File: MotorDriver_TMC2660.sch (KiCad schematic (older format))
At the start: 16 parts, among them U4 TMC2660

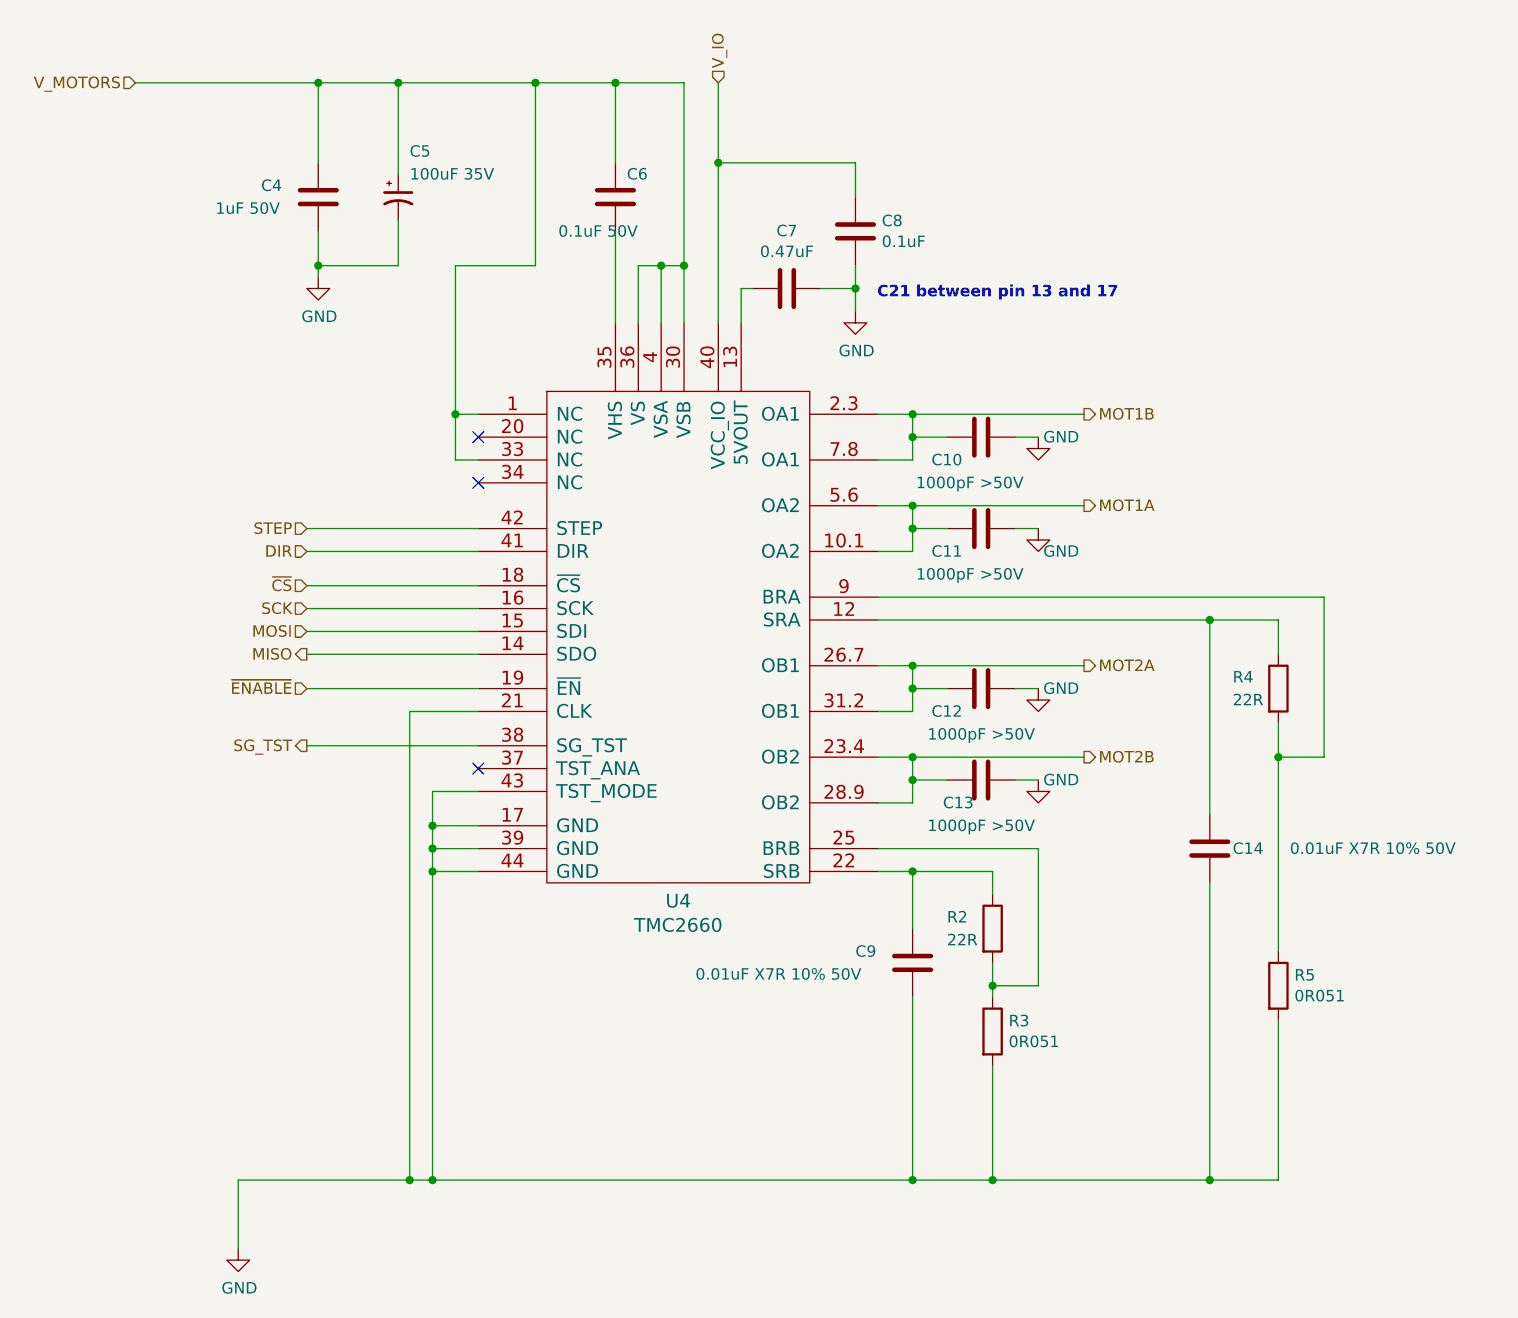
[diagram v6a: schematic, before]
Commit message: Routed most of the power traces.
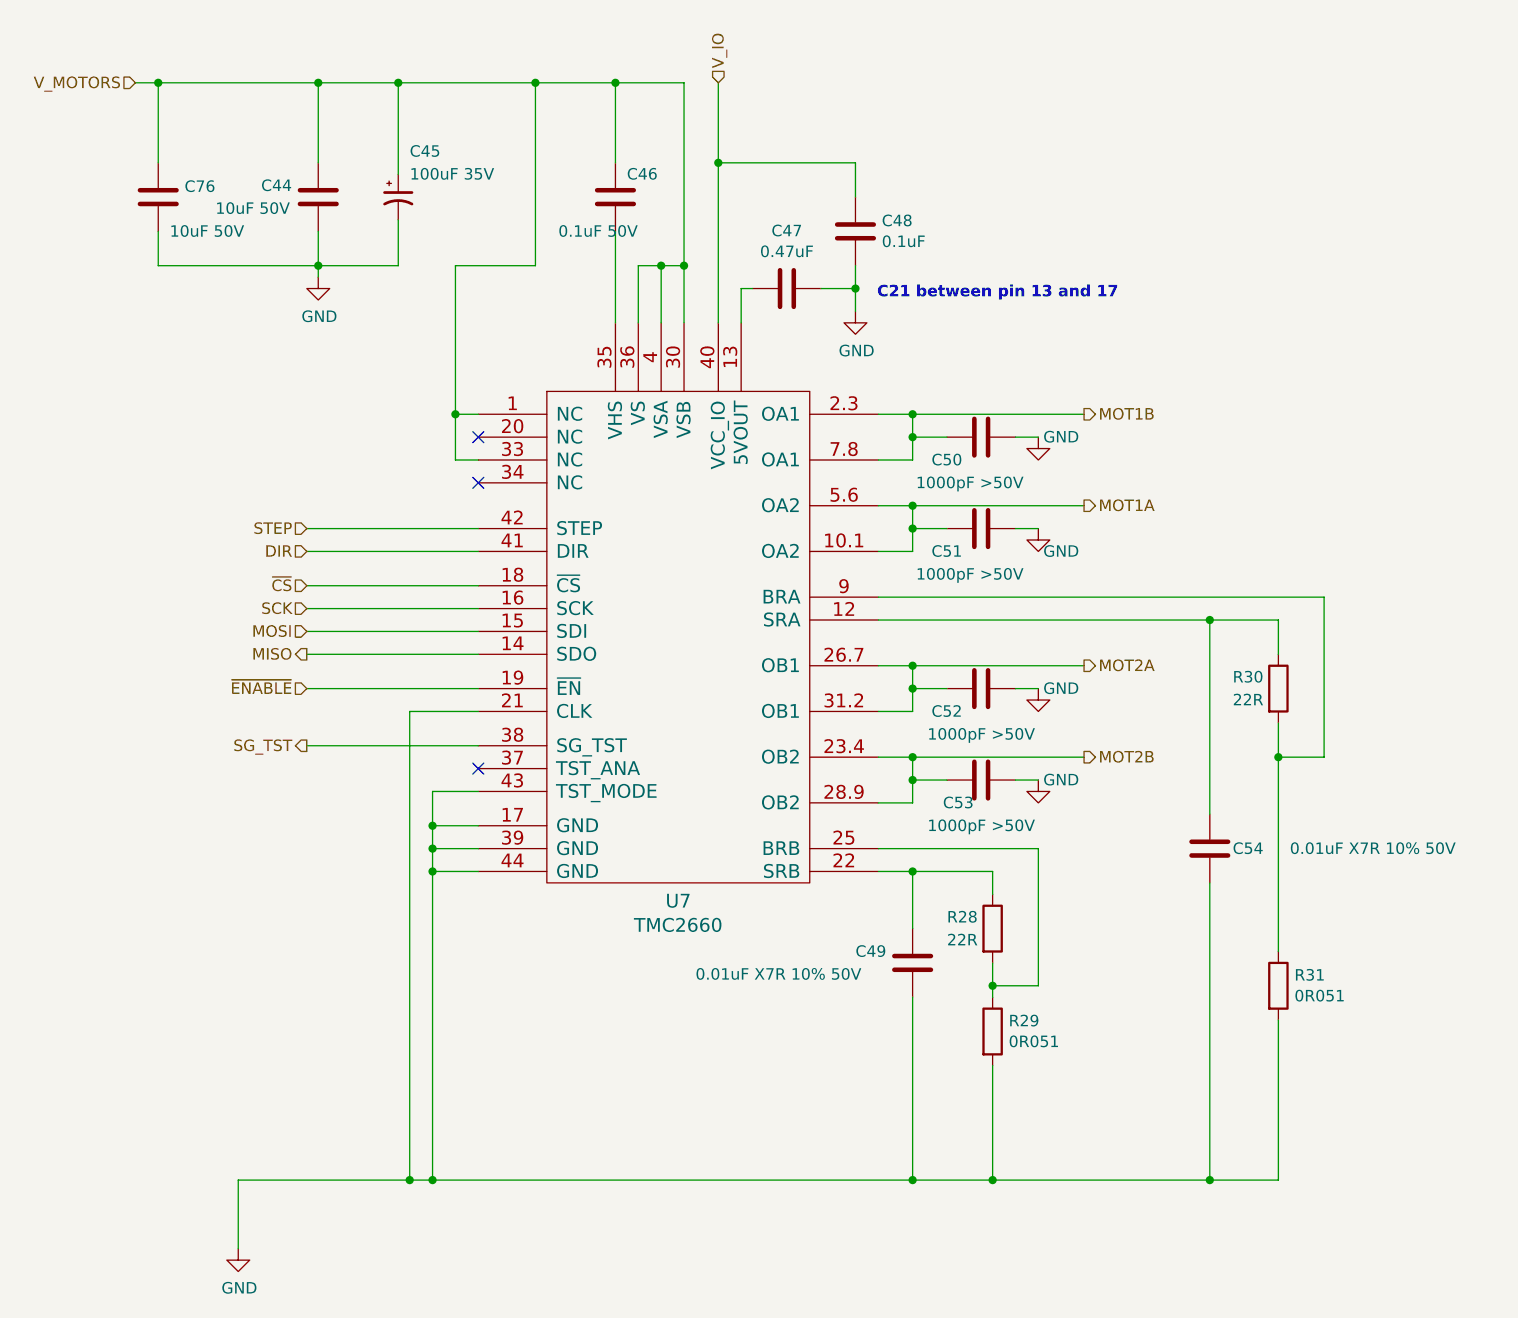
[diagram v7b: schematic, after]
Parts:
- added C74: 10uF 50V, Capacitor_SMD:C_1206_3216Metric, symbol Device:C
- C4: value 1uF 50V -> 10uF 50V; footprint Capacitor_SMD:C_0603_1608Metric -> Capacitor_SMD:C_1206_3216Metric
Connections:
- net GND: now also C74.2
- net V_MOTORS: now also C74.1
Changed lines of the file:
@@
 AR Path="/5AC337B6/5ACE1C6D/5ACC0B66/5AC338BF" Ref="U7"  Part="1"
 AR Path="/5AC337B6/5AD9F95A/5AD4B0F5/5AC338BF" Ref="U8"  Part="1"
-F 0 "U4" H 4875 2520 60  0000 C CNN
+F 0 "U7" H 4875 2520 60  0000 C CNN
 F 1 "TMC2660" H 4875 2414 60  0000 C CNN
 F 2 "PrntrBoardV1:TMC2660" H 4900 3600 60  0001 C CNN
@@
 AR Path="/5AC337B6/5ACE1C6D/5ACC0B66/5AC33A94" Ref="C46"  Part="1"
 AR Path="/5AC337B6/5AD9F95A/5AD4B0F5/5AC33A94" Ref="C59"  Part="1"
-F 0 "C6" H 4650 1800 50  0000 L CNN
+F 0 "C46" H 4650 1800 50  0000 L CNN
 F 1 "0.1uF 50V" H 4350 1550 50  0000 L CNN
 F 2 "Capacitor_SMD:C_0603_1608Metric" H 4638 1550 50  0001 C CNN
@@
 AR Path="/5AC337B6/5ACE1C6D/5ACC0B66/5AC33B3C" Ref="C44"  Part="1"
 AR Path="/5AC337B6/5AD9F95A/5AD4B0F5/5AC33B3C" Ref="C57"  Part="1"
-F 0 "C4" H 3050 1750 50  0000 L CNN
-F 1 "1uF 50V" H 2850 1650 50  0000 L CNN
-F 2 "Capacitor_SMD:C_0603_1608Metric" H 3338 1550 50  0001 C CNN
+F 0 "C44" H 3050 1750 50  0000 L CNN
+F 1 "10uF 50V" H 2850 1650 50  0000 L CNN
+F 2 "Capacitor_SMD:C_1206_3216Metric" H 3338 1550 50  0001 C CNN
 F 3 "~" H 3300 1700 50  0001 C CNN
 	1    3300 1700
@@
 AR Path="/5AC337B6/5ACE1C6D/5ACC0B66/5AC33B85" Ref="C47"  Part="1"
 AR Path="/5AC337B6/5AD9F95A/5AD4B0F5/5AC33B85" Ref="C60"  Part="1"
-F 0 "C7" V 5098 2100 50  0000 C CNN
+F 0 "C47" V 5098 2100 50  0000 C CNN
 F 1 "0.47uF" V 5189 2100 50  0000 C CNN
 F 2 "Capacitor_SMD:C_0603_1608Metric" H 5388 1950 50  0001 C CNN
@@
 AR Path="/5AC337B6/5ACE1C6D/5ACC0B66/5AC33C56" Ref="C48"  Part="1"
 AR Path="/5AC337B6/5AD9F95A/5AD4B0F5/5AC33C56" Ref="C61"  Part="1"
-F 0 "C8" H 5765 1896 50  0000 L CNN
+F 0 "C48" H 5765 1896 50  0000 L CNN
 F 1 "0.1uF" H 5765 1805 50  0000 L CNN
 F 2 "Capacitor_SMD:C_0603_1608Metric" H 5688 1700 50  0001 C CNN
@@
 AR Path="/5AC337B6/5ACE1C6D/5ACC0B66/5AC33CA1" Ref="C50"  Part="1"
 AR Path="/5AC337B6/5AD9F95A/5AD4B0F5/5AC33CA1" Ref="C63"  Part="1"
-F 0 "C10" V 6300 2600 50  0000 C CNN
+F 0 "C50" V 6300 2600 50  0000 C CNN
 F 1 "1000pF >50V" V 6400 2700 50  0000 C CNN
 F 2 "Capacitor_SMD:C_0603_1608Metric" H 6238 2600 50  0001 C CNN
@@
 AR Path="/5AC337B6/5ACE1C6D/5ACC0B66/5AC33D6E" Ref="C51"  Part="1"
 AR Path="/5AC337B6/5AD9F95A/5AD4B0F5/5AC33D6E" Ref="C64"  Part="1"
-F 0 "C11" V 6300 3000 50  0000 C CNN
+F 0 "C51" V 6300 3000 50  0000 C CNN
 F 1 "1000pF >50V" V 6400 3100 50  0000 C CNN
 F 2 "Capacitor_SMD:C_0603_1608Metric" H 6238 3000 50  0001 C CNN
@@
 AR Path="/5AC337B6/5ACE1C6D/5ACC0B66/5AC33DC1" Ref="C52"  Part="1"
 AR Path="/5AC337B6/5AD9F95A/5AD4B0F5/5AC33DC1" Ref="C65"  Part="1"
-F 0 "C12" V 6300 3700 50  0000 C CNN
+F 0 "C52" V 6300 3700 50  0000 C CNN
 F 1 "1000pF >50V" V 6400 3850 50  0000 C CNN
 F 2 "Capacitor_SMD:C_0603_1608Metric" H 6238 3700 50  0001 C CNN
@@
 AR Path="/5AC337B6/5ACE1C6D/5ACC0B66/5AC33E6E" Ref="C53"  Part="1"
 AR Path="/5AC337B6/5AD9F95A/5AD4B0F5/5AC33E6E" Ref="C66"  Part="1"
-F 0 "C13" V 6300 4150 50  0000 C CNN
+F 0 "C53" V 6300 4150 50  0000 C CNN
 F 1 "1000pF >50V" V 6400 4250 50  0000 C CNN
 F 2 "Capacitor_SMD:C_0603_1608Metric" H 6238 4100 50  0001 C CNN
@@
 AR Path="/5AC337B6/5ACE1C6D/5ACC0B66/5AC33EDF" Ref="C54"  Part="1"
 AR Path="/5AC337B6/5AD9F95A/5AD4B0F5/5AC33EDF" Ref="C67"  Part="1"
-F 0 "C14" H 7300 4550 50  0000 L CNN
+F 0 "C54" H 7300 4550 50  0000 L CNN
 F 1 "0.01uF X7R 10% 50V" H 7550 4550 50  0000 L CNN
 F 2 "Capacitor_SMD:C_0603_1608Metric" H 7238 4400 50  0001 C CNN
@@
 AR Path="/5AC337B6/5ACE1C6D/5ACC0B66/5AC33F7D" Ref="C49"  Part="1"
 AR Path="/5AC337B6/5AD9F95A/5AD4B0F5/5AC33F7D" Ref="C62"  Part="1"
-F 0 "C9" H 5650 5100 50  0000 L CNN
+F 0 "C49" H 5650 5100 50  0000 L CNN
 F 1 "0.01uF X7R 10% 50V" H 4950 5000 50  0000 L CNN
 F 2 "Capacitor_SMD:C_0603_1608Metric" H 5938 4900 50  0001 C CNN
@@
 AR Path="/5AC337B6/5ACE1C6D/5ACC0B66/5AC34593" Ref="#PWR049"  Part="1"
 AR Path="/5AC337B6/5AD9F95A/5AD4B0F5/5AC34593" Ref="#PWR059"  Part="1"
-F 0 "#PWR014" H 5650 1950 50  0001 C CNN
+F 0 "#PWR049" H 5650 1950 50  0001 C CNN
 F 1 "GND" H 5655 2027 50  0000 C CNN
 F 2 "" H 5650 2200 50  0001 C CNN
@@
 AR Path="/5AC337B6/5ACE1C6D/5ACC0B66/5AC345D6" Ref="#PWR048"  Part="1"
 AR Path="/5AC337B6/5AD9F95A/5AD4B0F5/5AC345D6" Ref="#PWR058"  Part="1"
-F 0 "#PWR013" H 3300 1800 50  0001 C CNN
+F 0 "#PWR048" H 3300 1800 50  0001 C CNN
 F 1 "GND" H 3305 1877 50  0000 C CNN
 F 2 "" H 3300 2050 50  0001 C CNN
@@
 AR Path="/5AC337B6/5ACE1C6D/5ACC0B66/5AC34619" Ref="#PWR050"  Part="1"
 AR Path="/5AC337B6/5AD9F95A/5AD4B0F5/5AC34619" Ref="#PWR060"  Part="1"
-F 0 "#PWR015" H 6450 2500 50  0001 C CNN
+F 0 "#PWR050" H 6450 2500 50  0001 C CNN
 F 1 "GND" H 6550 2750 50  0000 C CNN
 F 2 "" H 6450 2750 50  0001 C CNN
@@
 AR Path="/5AC337B6/5ACE1C6D/5ACC0B66/5AC3465C" Ref="#PWR051"  Part="1"
 AR Path="/5AC337B6/5AD9F95A/5AD4B0F5/5AC3465C" Ref="#PWR061"  Part="1"
-F 0 "#PWR016" H 6450 2900 50  0001 C CNN
+F 0 "#PWR051" H 6450 2900 50  0001 C CNN
 F 1 "GND" H 6550 3050 50  0000 C CNN
 F 2 "" H 6450 3150 50  0001 C CNN
@@
 AR Path="/5AC337B6/5ACE1C6D/5ACC0B66/5AC3469F" Ref="#PWR052"  Part="1"
 AR Path="/5AC337B6/5AD9F95A/5AD4B0F5/5AC3469F" Ref="#PWR062"  Part="1"
-F 0 "#PWR017" H 6450 3600 50  0001 C CNN
+F 0 "#PWR052" H 6450 3600 50  0001 C CNN
 F 1 "GND" H 6550 3850 50  0000 C CNN
 F 2 "" H 6450 3850 50  0001 C CNN
@@
 AR Path="/5AC337B6/5ACE1C6D/5ACC0B66/5AC346E2" Ref="#PWR053"  Part="1"
 AR Path="/5AC337B6/5AD9F95A/5AD4B0F5/5AC346E2" Ref="#PWR063"  Part="1"
-F 0 "#PWR018" H 6450 4000 50  0001 C CNN
+F 0 "#PWR053" H 6450 4000 50  0001 C CNN
 F 1 "GND" H 6550 4250 50  0000 C CNN
 F 2 "" H 6450 4250 50  0001 C CNN
@@
 AR Path="/5AC337B6/5ACE1C6D/5ACC0B66/5AC34725" Ref="#PWR047"  Part="1"
 AR Path="/5AC337B6/5AD9F95A/5AD4B0F5/5AC34725" Ref="#PWR057"  Part="1"
-F 0 "#PWR012" H 2950 6050 50  0001 C CNN
+F 0 "#PWR047" H 2950 6050 50  0001 C CNN
 F 1 "GND" H 2955 6127 50  0000 C CNN
 F 2 "" H 2950 6300 50  0001 C CNN
@@
 Connection ~ 3300 1200
 Wire Wire Line
-	3300 1200 2500 1200
+	3300 1200 2600 1200
 Wire Wire Line
 	3300 1850 3300 2000
@@
 AR Path="/5AC337B6/5ACE1C6D/5ACC0B66/5AC3912E" Ref="R28"  Part="1"
 AR Path="/5AC337B6/5AD9F95A/5AD4B0F5/5AC3912E" Ref="R36"  Part="1"
-F 0 "R2" H 6050 4950 50  0000 L CNN
+F 0 "R28" H 6050 4950 50  0000 L CNN
 F 1 "22R" H 6050 4850 50  0000 L CNN
 F 2 "Resistor_SMD:R_0603_1608Metric" V 6180 4900 50  0001 C CNN
@@
 AR Path="/5AC337B6/5ACE1C6D/5ACC0B66/5AC391BE" Ref="R29"  Part="1"
 AR Path="/5AC337B6/5AD9F95A/5AD4B0F5/5AC391BE" Ref="R37"  Part="1"
-F 0 "R3" H 6320 5396 50  0000 L CNN
+F 0 "R29" H 6320 5396 50  0000 L CNN
 F 1 "0R051" H 6320 5305 50  0000 L CNN
 F 2 "Resistor_SMD:R_1206_3216Metric" V 6180 5350 50  0001 C CNN
@@
 AR Path="/5AC337B6/5ACE1C6D/5ACC0B66/5AC3921D" Ref="R30"  Part="1"
 AR Path="/5AC337B6/5AD9F95A/5AD4B0F5/5AC3921D" Ref="R38"  Part="1"
-F 0 "R4" H 7300 3900 50  0000 L CNN
+F 0 "R30" H 7300 3900 50  0000 L CNN
 F 1 "22R" H 7300 3800 50  0000 L CNN
 F 2 "Resistor_SMD:R_0603_1608Metric" V 7430 3850 50  0001 C CNN
@@
 AR Path="/5AC337B6/5ACE1C6D/5ACC0B66/5AC392A1" Ref="R31"  Part="1"
 AR Path="/5AC337B6/5AD9F95A/5AD4B0F5/5AC392A1" Ref="R39"  Part="1"
-F 0 "R5" H 7570 5196 50  0000 L CNN
+F 0 "R31" H 7570 5196 50  0000 L CNN
 F 1 "0R051" H 7570 5105 50  0000 L CNN
 F 2 "Resistor_SMD:R_1206_3216Metric" V 7430 5150 50  0001 C CNN
@@
 AR Path="/5AC337B6/5ACE1C6D/5ACC0B66/5AC55FA7" Ref="C45"  Part="1"
 AR Path="/5AC337B6/5AD9F95A/5AD4B0F5/5AC55FA7" Ref="C58"  Part="1"
-F 0 "C5" H 3700 1900 50  0000 L CNN
+F 0 "C45" H 3700 1900 50  0000 L CNN
 F 1 "100uF 35V" H 3700 1800 50  0000 L CNN
 F 2 "Capacitor_SMD:CP_Elec_6.3x7.7" H 3650 1700 50  0001 C CNN
@@
 Wire Wire Line
 	6350 3150 6450 3150
+$Comp
+L Device:C C74
+U 1 1 5ACA36B2
+P 2600 1700
+AR Path="/5AC337B6/5ACC0AA2/5ACC0B66/5ACA36B2" Ref="C74"  Part="1"
+AR Path="/5AC337B6/5ACBE919/5AD4B0F5/5ACA36B2" Ref="C73"  Part="1"
+AR Path="/5AC337B6/5ACCA309/5ACC0B66/5ACA36B2" Ref="C75"  Part="1"
+AR Path="/5AC337B6/5ACE1C6D/5ACC0B66/5ACA36B2" Ref="C76"  Part="1"
+AR Path="/5AC337B6/5AD9F95A/5AD4B0F5/5ACA36B2" Ref="C77"  Part="1"
+F 0 "C76" H 2715 1746 50  0000 L CNN
+F 1 "10uF 50V" H 2650 1550 50  0000 L CNN
+F 2 "Capacitor_SMD:C_1206_3216Metric" H 2638 1550 50  0001 C CNN
+F 3 "~" H 2600 1700 50  0001 C CNN
+	1    2600 1700
+	1    0    0    -1
+$EndComp
+Wire Wire Line
+	2600 1550 2600 1200
+Connection ~ 2600 1200
+Wire Wire Line
+	2600 1200 2500 1200
+Wire Wire Line
+	2600 1850 2600 2000
+Wire Wire Line
+	2600 2000 3300 2000
 $EndSCHEMATC

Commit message: Updated schematics with the latest features.
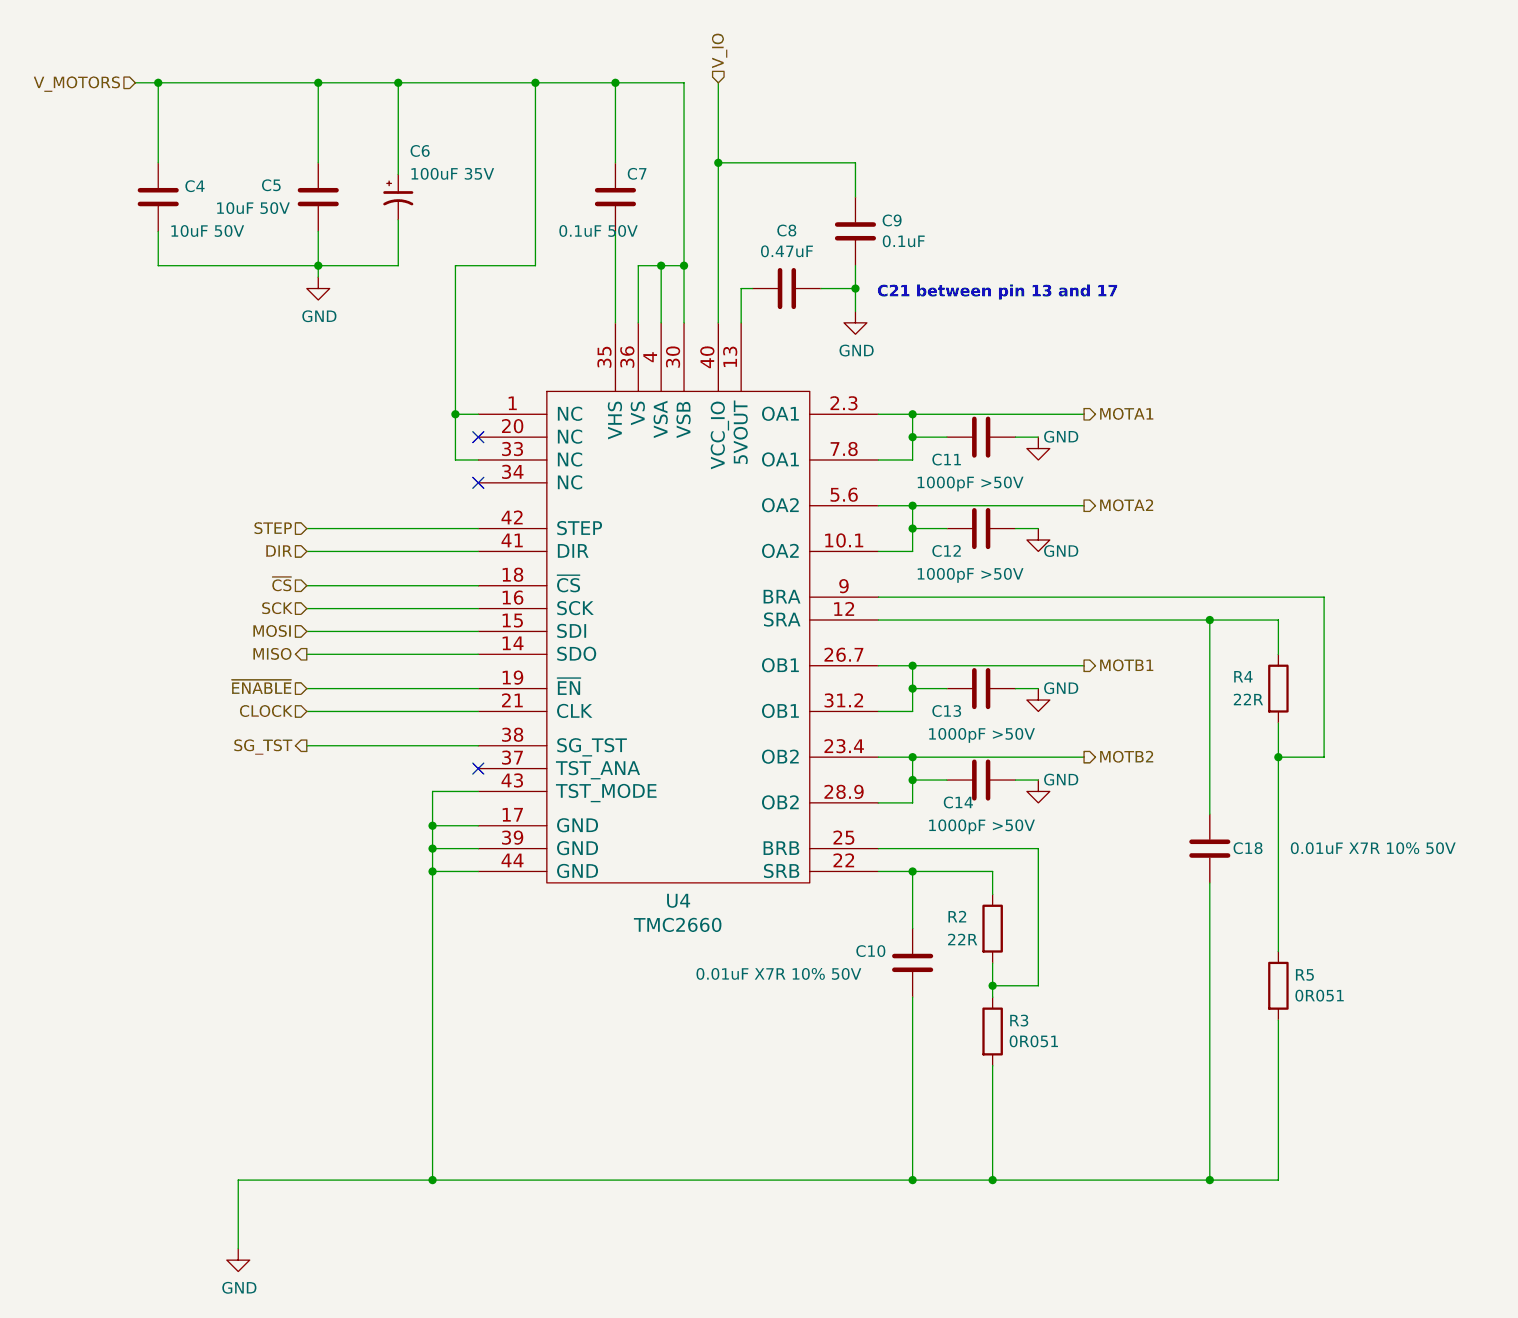
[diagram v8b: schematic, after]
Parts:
- renumbered C9 to C10, C10 to C11, C11 to C12, C12 to C13, C13 to C14, C14 to C18, C74 to C4, C4 to C5, C5 to C6, C6 to C7, C7 to C8, C8 to C9
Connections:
- net GND: no longer U4.21 (CLK)
- net MOT1A renamed MOTA2
- net MOT1B renamed MOTA1
- net MOT2A renamed MOTB1
- net MOT2B renamed MOTB2
- new net CLOCK: U4.21 (CLK)
